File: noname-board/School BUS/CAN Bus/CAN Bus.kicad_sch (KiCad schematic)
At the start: 0 parts

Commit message: CAN booos
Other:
- sheet CAN Bus ports: added none; removed data_0, data_1
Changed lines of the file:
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@@
       (effects (font (size 1.27 1.27)) (justify left top))
-    )
-    (pin "data_0" input (at 182.88 123.19 0)
-      (effects (font (size 1.27 1.27)) (justify right))
-    )
-    (pin "data_1" input (at 182.88 127 0)
-      (effects (font (size 1.27 1.27)) (justify right))
     )
     (instances

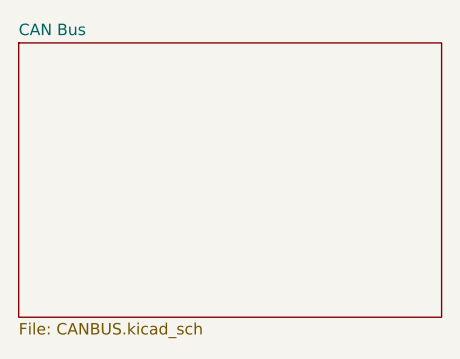
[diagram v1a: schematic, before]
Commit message: Update CAN Bus.kicad_sch
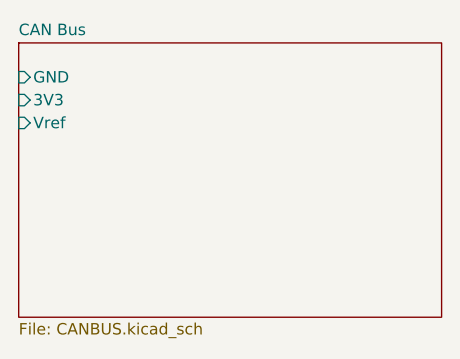
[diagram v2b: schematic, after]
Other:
- sheet CAN Bus ports: added 3V3, GND, Vref; removed none
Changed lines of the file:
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@@
       (effects (font (size 1.27 1.27)) (justify left top))
+    )
+    (pin "GND" input (at 135.89 123.19 180)
+      (effects (font (size 1.27 1.27)) (justify left))
+    )
+    (pin "3V3" input (at 135.89 125.73 180)
+      (effects (font (size 1.27 1.27)) (justify left))
+    )
+    (pin "Vref" input (at 135.89 128.27 180)
+      (effects (font (size 1.27 1.27)) (justify left))
     )
     (instances
